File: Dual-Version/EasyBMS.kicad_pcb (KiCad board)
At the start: 2 copper layers, 48.8 x 100 mm, 174 parts, among them IC1 XL7046, IC2 LTC6811IG-1#PBF, IC3 ISO1042DWV, IC4 AMS1117-3.3, J1 TYPE-C-31-M-12, Q14 CJ2301, Q15 CJ2301, Q16 CJ2301, Q18 CJ2301, Q20 CJ2301, Q22 CJ2301, Q24 CJ2301, Q26 CJ2301, Q28 CJ2301, Q30 CJ2301, Q32 CJ2301, Q34 CJ2301, U1 ESP32-C6-MINI-1-N4, Y1 FC-135_32.7680KA-A5

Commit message: schematic improvements, parts changed, layout progress
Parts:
- removed CSLTC0, MISO0: SJ, EasyBMS:SJ_252
- removed IC3: ISO1042DWV, EasyBMS:SOIC127P1150X280-8N
- removed JP7: 2828XX-4282834-4, EasyBMS:TERMBLK_254-4N_16378166
- added B1: ~, RS485 Modul:RS-485-MODULE, F.Cu at (112.3, -18.5)
- added C18: 22uF, EasyBMS:C0805_334, F.Cu at (79.1, 54.8)
- added C22: 100nF, EasyBMS:C0402_334, F.Cu at (165.1, 15.1)
- added C30: 10nF, EasyBMS:C0402_334, F.Cu at (164.9, 127.2)
- added C32: 10nF, EasyBMS:C0402_334, F.Cu at (164.9, 121.3)
- added C34: 10nF, EasyBMS:C0402_334, F.Cu at (164.9, 115.4)
- added C36: 10nF, EasyBMS:C0402_334, F.Cu at (164.9, 109.5)
- added C38: 10nF, EasyBMS:C0402_334, F.Cu at (164.9, 103.6)
- added C40: 10nF, EasyBMS:C0402_334, F.Cu at (164.9, 97.7)
- added C42: 10nF, EasyBMS:C0402_334, F.Cu at (138.6, 96.1)
- added C44: 10nF, EasyBMS:C0402_334, F.Cu at (164.9, 91.8)
- added C46: 10nF, EasyBMS:C0402_334, F.Cu at (164.9, 85.9)
- added C48: 10nF, EasyBMS:C0402_334, F.Cu at (164.9, 80.0)
- added C49: 10nF, EasyBMS:C0402_334, F.Cu at (164.9, 74.1)
- added C50: 10nF, EasyBMS:C0402_334, F.Cu at (164.9, 68.2)
- added C51: 10nF, EasyBMS:C0402_334, F.Cu at (145.6, 94.8)
- added C52: 100nF, EasyBMS:C0805_334, F.Cu at (156.7, 109.9)
- added C53: 1uF, EasyBMS:C0402_334, F.Cu at (145.5, 98.8)
- added C54: 1uF, EasyBMS:C0402_334, F.Cu at (145.5, 100.1)
- added C55: 1uF, EasyBMS:C0402_334, F.Cu at (145.4, 101.3)
- added C56: 10nF, EasyBMS:C0402_334, F.Cu at (142.8, 104.8)
- added C57: 10nF, EasyBMS:C0805_334, F.Cu at (141.1, 100.2)
- added C58: 10nF, EasyBMS:C0805_334, F.Cu at (141.1, 102.2)
- added C59: 100nF, EasyBMS:C0805_334, F.Cu at (155.9, 114.8)
- added C61: 100nF, EasyBMS:C0402_334, F.Cu at (165.1, 19.2)
- added C62: 100nF, EasyBMS:C0402_334, F.Cu at (79.2, 30.0)
- added C64: 22uF, EasyBMS:C0805_334, F.Cu at (79.1, 57.9)
- added C65: 22uF, EasyBMS:C0805_334, F.Cu at (83.1, 29.9)
- added C66: 10nF, EasyBMS:C0402_334, F.Cu at (133.9, 93.3)
- added CAN-GNDP1: SJ, EasyBMS:SJ_252, F.Cu at (156.6, -22.3)
- added CAN-GNDV1: SJ, EasyBMS:SJ_252, F.Cu at (156.5, -17.6)
- added CAN-HP1: SJ, EasyBMS:SJ_252, F.Cu at (156.4, -14.0)
- added CAN-HV1: SJ, EasyBMS:SJ_252, F.Cu at (156.0, -10.2)
- added CAN-LP1: SJ, EasyBMS:SJ_252, F.Cu at (156.1, -6.30)
- added CAN-LV1: SJ, EasyBMS:SJ_252, F.Cu at (170.4, -16.8)
- added D17: ZMM5V6, EasyBMS:MELF-MLL34, F.Cu at (162.6, 133.1)
- added D19: ZMM5V6, EasyBMS:MELF-MLL34, F.Cu at (162.6, 127.2)
- added D21: ZMM5V6, EasyBMS:MELF-MLL34, F.Cu at (162.6, 121.3)
- added D23: ZMM5V6, EasyBMS:MELF-MLL34, F.Cu at (162.6, 115.4)
- added D25: ZMM5V6, EasyBMS:MELF-MLL34, F.Cu at (162.6, 109.5)
- added D26: ZMM5V6, EasyBMS:MELF-MLL34, F.Cu at (162.6, 103.6)
- added D27: ZMM5V6, EasyBMS:MELF-MLL34, F.Cu at (162.6, 97.7)
- added D28: ZMM5V6, EasyBMS:MELF-MLL34, F.Cu at (162.6, 91.8)
- added D29: ZMM5V6, EasyBMS:MELF-MLL34, F.Cu at (162.6, 85.9)
- added D30: ZMM5V6, EasyBMS:MELF-MLL34, F.Cu at (162.6, 80.0)
- added D31: ZMM5V6, EasyBMS:MELF-MLL34, F.Cu at (162.6, 74.1)
- added D32: ZMM5V6, EasyBMS:MELF-MLL34, F.Cu at (162.6, 68.2)
- added D33: SS210, EasyBMS:DO214AC_210, F.Cu at (156.0, 68.8)
- added D34: SS210, EasyBMS:DO214AC_210, F.Cu at (156.0, 71.3)
- added D35: PESD5V0L1BA, Diode_SMD:D_SOD-323, F.Cu at (161.0, 15.6)
- added D36: PESD5V0L1BA, Diode_SMD:D_SOD-323, F.Cu at (161.0, 18.5)
- added D37: LESD5D5.0CT1G, Diode_SMD:D_SOD-523, F.Cu at (72.8, 34.5)
- added D38: PESD5V0L1BA, Diode_SMD:D_SOD-323, F.Cu at (161.0, 21.5)
- added F1: 60V 100mA/JK-NSMD010, Resistor_SMD:R_1206_3216Metric, F.Cu at (169.9, 15.8)
- added F2: 60V 100mA/JK-NSMD010, Resistor_SMD:R_1206_3216Metric, F.Cu at (169.9, 19.1)
- added GND1: SJ, EasyBMS:SJ_252, F.Cu at (159.1, 66.4)
- added GND2: SJ, EasyBMS:SJ_252, F.Cu at (121.0, 136.2)
- added H4: MountingHole_Pad, MountingHole:MountingHole_6.5mm_Pad_Via, F.Cu at (151.6, 130.3)
- added H5: MountingHole_Pad, MountingHole:MountingHole_6.5mm_Pad_Via, F.Cu at (135.6, 130.3)
- added IC5: LTC6811IG-1, EasyBMS:SOP50P780X200-48N, F.Cu at (152.0, 100.6)
- added IC6: AMS1117-5, EasyBMS:SOT223_111, F.Cu at (79.3, -33.6)
- added IP-/GND1: SJ, EasyBMS:SJ_252, F.Cu at (124.8, 128.4)
- added J2: Screw_Terminal_01x04, TerminalBlock_TE-Connectivity:TerminalBlock_TE_282834-4_1x04_P2.54mm_Horizontal, F.Cu at (153.2, 18.0)
- added JP14: PINHD-1X2, EasyBMS:1X02, F.Cu at (186.2, 108.5)
- added JP15: PINHD-1X2, EasyBMS:1X02, F.Cu at (186.2, 105.5)
- added JP16: PINHD-1X2, EasyBMS:1X02, F.Cu at (186.2, 102.5)
- added JP17: PINHD-1X2, EasyBMS:1X02, F.Cu at (186.2, 99.5)
- added JP18: PINHD-1X2, EasyBMS:1X02, F.Cu at (186.2, 96.5)
- added JP19: PINHD-1X2, EasyBMS:1X02, F.Cu at (186.2, 93.5)
- added JP20: PINHD-1X2, EasyBMS:1X02, F.Cu at (186.2, 90.5)
- added JP21: PINHD-1X2, EasyBMS:1X02, F.Cu at (186.2, 87.5)
- added JP22: PINHD-1X2, EasyBMS:1X02, F.Cu at (186.2, 84.5)
- added JP23: PINHD-1X2, EasyBMS:1X02, F.Cu at (186.2, 81.5)
- added JP24: PINHD-1X2, EasyBMS:1X02, F.Cu at (186.2, 78.5)
- added Q1: CJ2301, EasyBMS:PG-SOT-23, F.Cu at (167.4, 133.1)
- added Q10: CJ2301, EasyBMS:PG-SOT-23, F.Cu at (167.4, 80.0)
- added Q11: CJ2301, EasyBMS:PG-SOT-23, F.Cu at (167.4, 74.1)
- added Q12: CJ2301, EasyBMS:PG-SOT-23, F.Cu at (167.4, 68.2)
- added Q13: NSV1C201MZ4, Package_TO_SOT_SMD:SOT-223, F.Cu at (150.1, 112.0)
- added Q2: CJ2301, EasyBMS:PG-SOT-23, F.Cu at (167.4, 127.2)
- added Q3: CJ2301, EasyBMS:PG-SOT-23, F.Cu at (167.4, 121.3)
- added Q4: CJ2301, EasyBMS:PG-SOT-23, F.Cu at (167.4, 115.4)
- added Q5: CJ2301, EasyBMS:PG-SOT-23, F.Cu at (167.4, 109.5)
- added Q6: CJ2301, EasyBMS:PG-SOT-23, F.Cu at (167.4, 103.6)
- added Q7: CJ2301, EasyBMS:PG-SOT-23, F.Cu at (167.4, 97.7)
- added Q8: CJ2301, EasyBMS:PG-SOT-23, F.Cu at (167.4, 91.8)
- added Q9: CJ2301, EasyBMS:PG-SOT-23, F.Cu at (167.4, 85.9)
- added R22: 49R9, EasyBMS:R0603_334, F.Cu at (135.4, 94.9)
- added R23: 1k, EasyBMS:R0603_334, F.Cu at (133.9, 97.7)
- added R24: 10k, EasyBMS:R0402_334, F.Cu at (141.1, 96.1)
- added R25: 10R0, EasyBMS:R1206_334, F.Cu at (178.6, 133.1)
- added R26: 10R0, EasyBMS:R1206_334, F.Cu at (178.6, 127.2)
- added R27: 10R0, EasyBMS:R1206_334, F.Cu at (178.6, 121.3)
- added R28: 10R0, EasyBMS:R1206_334, F.Cu at (178.6, 115.4)
- added R29: 10R0, EasyBMS:R1206_334, F.Cu at (178.6, 109.5)
- added R30: 10R0, EasyBMS:R1206_334, F.Cu at (178.6, 103.6)
- added R31: 10R0, EasyBMS:R1206_334, F.Cu at (178.6, 97.7)
- added R32: 10R0, EasyBMS:R1206_334, F.Cu at (178.6, 91.8)
- added R33: 10R0, EasyBMS:R1206_334, F.Cu at (178.6, 85.9)
- added R34: 10R0, EasyBMS:R1206_334, F.Cu at (178.6, 80.0)
- added R35: 10R0, EasyBMS:R1206_334, F.Cu at (178.6, 74.1)
- added R36: 10R0, EasyBMS:R1206_334, F.Cu at (178.6, 68.2)
- added R37: 10R0, EasyBMS:R1206_334, F.Cu at (171.4, 133.1)
- added R38: 10R0, EasyBMS:R1206_334, F.Cu at (171.4, 127.2)
- added R39: 10R0, EasyBMS:R1206_334, F.Cu at (171.4, 121.3)
- added R40: 10R0, EasyBMS:R1206_334, F.Cu at (171.4, 115.4)
- added R41: 10R0, EasyBMS:R1206_334, F.Cu at (171.4, 109.5)
- added R42: 10R0, EasyBMS:R1206_334, F.Cu at (171.4, 103.6)
- added R43: 10R0, EasyBMS:R1206_334, F.Cu at (171.4, 97.7)
- added R44: 10R0, EasyBMS:R1206_334, F.Cu at (171.4, 91.8)
- added R45: 10R0, EasyBMS:R1206_334, F.Cu at (171.4, 85.9)
- added R46: 10R0, EasyBMS:R1206_334, F.Cu at (171.4, 80.0)
- added R47: 10R0, EasyBMS:R1206_334, F.Cu at (171.4, 74.1)
- added R48: 10R0, EasyBMS:R1206_334, F.Cu at (171.4, 68.2)
- added R49: 100R, EasyBMS:R0402_334, F.Cu at (165.7, 135.2)
- added R50: 100R, EasyBMS:R0402_334, F.Cu at (165.7, 129.3)
- added R51: 100R, EasyBMS:R0402_334, F.Cu at (165.7, 123.4)
- added R52: 100R, EasyBMS:R0402_334, F.Cu at (165.7, 117.5)
- added R53: 100R, EasyBMS:R0402_334, F.Cu at (165.7, 111.6)
- added R54: 100R, EasyBMS:R0402_334, F.Cu at (165.7, 105.7)
- added R56: 100R, EasyBMS:R0402_334, F.Cu at (165.7, 99.8)
- added R62: 100R, EasyBMS:R0402_334, F.Cu at (165.7, 93.9)
- added R63: 100R, EasyBMS:R0402_334, F.Cu at (165.7, 88.0)
- added R64: 100R, EasyBMS:R0402_334, F.Cu at (165.7, 82.1)
- added R65: 100R, EasyBMS:R0402_334, F.Cu at (165.7, 76.2)
- added R66: 100R, EasyBMS:R0402_334, F.Cu at (165.7, 70.3)
- added R67: 3.3k, EasyBMS:R0402_334, F.Cu at (165.7, 131.0)
- added R68: 3.3k, EasyBMS:R0402_334, F.Cu at (165.7, 125.1)
- added R69: 3.3k, EasyBMS:R0402_334, F.Cu at (165.7, 119.2)
- added R70: 3.3k, EasyBMS:R0402_334, F.Cu at (165.7, 113.3)
- added R71: 3.3k, EasyBMS:R0402_334, F.Cu at (165.7, 107.4)
- added R72: 3.3k, EasyBMS:R0402_334, F.Cu at (165.7, 101.5)
- added R73: 3.3k, EasyBMS:R0402_334, F.Cu at (165.7, 95.6)
- added R74: 3.3k, EasyBMS:R0402_334, F.Cu at (165.7, 89.7)
- added R75: 3.3k, EasyBMS:R0402_334, F.Cu at (165.7, 83.8)
- added R76: 3.3k, EasyBMS:R0402_334, F.Cu at (165.7, 77.9)
- added R77: 3.3k, EasyBMS:R0402_334, F.Cu at (165.7, 72.0)
- added R78: 3.3k, EasyBMS:R0402_334, F.Cu at (165.7, 66.1)
- added R80: 100R, EasyBMS:R0402_334, F.Cu at (159.8, 69.1)
- added R81: 10k, EasyBMS:R0603_334, F.Cu at (182.1, 128.0)
- added R83: 10k NTC, EasyBMS:R0603_334, F.Cu at (182.1, 131.7)
- added R84: 12k, EasyBMS:R0402_334, F.Cu at (145.6, 97.0)
- added R85: 12k, EasyBMS:R0402_334, F.Cu at (145.6, 95.9)
- added R86: 10k, EasyBMS:R0603_334, F.Cu at (182.2, 79.6)
- added R87: 10k NTC, EasyBMS:R0603_334, F.Cu at (182.2, 76.4)
- added R88: 100R, EasyBMS:R0402_334, F.Cu at (156.2, 108.2)
- added R89: 1k, EasyBMS:R0603_334, F.Cu at (145.4, 107.8)
- added R90: 100R, EasyBMS:R0603_334, F.Cu at (144.9, 110.4)
- added R91: 1k, EasyBMS:R0603_334, F.Cu at (143.3, 107.8)
- added R92: 49R9, EasyBMS:R0603_334, F.Cu at (144.9, 105.0)
- added R93: 49R9, EasyBMS:R0603_334, F.Cu at (144.9, 102.9)
- added RS485-AP1: SJ, EasyBMS:SJ_252, F.Cu at (170.4, -13.6)
- added RS485-BP1: SJ, EasyBMS:SJ_252, F.Cu at (170.4, -10.4)
- added RS485-GNDPWR1: SJ, EasyBMS:SJ_252, F.Cu at (157.1, 51.8)
- added RS485-VDD1: SJ, EasyBMS:SJ_252, F.Cu at (170.4, -4.08)
- added U2: ACS770xCB-100B-PFF, Sensor_Current:Allegro_CB_PFF, B.Cu at (137.9, 98.3)
- added U3: ADuM1201BR, Package_SO:SOIC-8_3.9x4.9mm_P1.27mm, F.Cu at (70.8, 30.1)
- added U4: RJ-064-1, RJ45 Connectors:CONN-SMD_RJ-064, F.Cu at (149.0, 44.7)
- added U5: CA-IS3050CG, Package_SO:SOIC-8_7.5x5.85mm_P1.27mm, F.Cu at (143.9, 20.5)
- added U6: RJ-064-1, RJ45 Connectors:CONN-SMD_RJ-064, F.Cu at (165.3, 44.7)
- added U7: TME-0305S, Converter_DCDC:Converter_DCDC_TRACO_TME_03xxS_05xxS_12xxS_Single_THT, F.Cu at (129.2, 20.2)
- C12: value 47µF -> 22uF; footprint EasyBMS:C1206_334 -> EasyBMS:C0805_334
- C2: value 100µF/16V -> 10uF; footprint EasyBMS:153CLV-0605_334 -> Capacitor_SMD:C_0805_2012Metric
- C3: value 100nF -> 10nF
- C7: value 1uF -> 22uF; footprint EasyBMS:C0402_334 -> EasyBMS:C0805_334
- IC2: value LTC6811IG-1#PBF -> LTC6811IG-1
- R1: value 100R -> 49R9
- R17: value 20k -> 1k
- R59: value 600R@100MHz -> 100R
- moved C11 118.1 mm to (148.6, 24.3)
- moved R12 117.9 mm to (150.2, 28.7)
- moved TERM0 117.8 mm to (152.6, 28.7)
- moved C10 114.5 mm to (136.1, 20.4)
- moved H2 110.9 mm to (186.3, 41.5)
- moved C2 109.9 mm to (96.9, 15.8)
- moved D7 65.9 mm to (124.2, 133.8), turned to 180 degrees
- moved C12 65.7 mm to (129.7, 89.5), turned to 180 degrees
- moved D1 62.4 mm to (124.2, 131.3), turned to 0 degrees
- moved C3 50.3 mm to (164.9, 133.1)
- moved R59 41.1 mm to (156.4, 112.7), turned to 180 degrees
- moved R1 40.4 mm to (132.4, 94.9), turned to 180 degrees
- moved R57 38.5 mm to (134.6, 105.6)
- moved R4 38.1 mm to (98.0, 70.9)
- moved R7 38.1 mm to (98.0, 123.0)
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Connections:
- net +5V/1 renamed +12V
- net /C0 renamed /Cell Pack 1/C0
- net /C1 renamed /Cell Pack 1/C1
- net /C1+ renamed /Cell Pack 1/C1+
- net /C10 renamed /Cell Pack 1/C10
- net /C10+ renamed /Cell Pack 1/C10+
- net /C11 renamed /Cell Pack 1/C11
- net /C11+ renamed /Cell Pack 1/C11+
- net /C12 renamed /Cell Pack 1/C12
- net /C12+ renamed /Cell Pack 1/C12+
- net /C2 renamed /Cell Pack 1/C2
- net /C2+ renamed /Cell Pack 1/C2+
- net /C3 renamed /Cell Pack 1/C3
- net /C3+ renamed /Cell Pack 1/C3+
- net /C4 renamed /Cell Pack 1/C4
- net /C4+ renamed /Cell Pack 1/C4+
- net /C5 renamed /Cell Pack 1/C5
- net /C5+ renamed /Cell Pack 1/C5+
- net /C6 renamed /Cell Pack 1/C6
- net /C6+ renamed /Cell Pack 1/C6+
- net /C7 renamed /Cell Pack 1/C7
- net /C7+ renamed /Cell Pack 1/C7+
- net /C8 renamed /Cell Pack 1/C8
- net /C8+ renamed /Cell Pack 1/C8+
- net /C9 renamed /Cell Pack 1/C9
- net /C9+ renamed /Cell Pack 1/C9+
- net /CSLTC renamed CSLTC
- net /IPB renamed /Cell Pack 1/IPB
- net /MISO renamed MISO
- net /MOSI renamed MOSI
- net /S1 renamed /Cell Pack 1/S1
- net /S10 renamed /Cell Pack 1/S10
- net /S11 renamed /Cell Pack 1/S11
- net /S12 renamed /Cell Pack 1/S12
- net /S2 renamed /Cell Pack 1/S2
- net /S3 renamed /Cell Pack 1/S3
- net /S4 renamed /Cell Pack 1/S4
- net /S5 renamed /Cell Pack 1/S5
- net /S6 renamed /Cell Pack 1/S6
- net /S7 renamed /Cell Pack 1/S7
- net /S8 renamed /Cell Pack 1/S8
- net /S9 renamed /Cell Pack 1/S9
- net /SCLK renamed SCLK
- net /V+ renamed /Cell Pack 1/V+
- net /VREF1 renamed /Cell Pack 1/VREF1
- net /VREF2 renamed /Cell Pack 1/VREF2
- net /VTEMP2 renamed /Cell Pack 1/VTEMP2
- C1 pad 2: /GND2 -> GND
- C11 pad 1: Net-(IC3-VCC2) -> Net-(D37-K)
- C11 pad 2: Net-(IC3-GND2) -> Net-(D35-A1)
- C12 pad 1: Net-(IC3-VCC2) -> +5V
- C12 pad 2: Net-(IC3-GND2) -> GND
- C19 pad 2: /GND2 -> GND
- C20 pad 1: /GND2 -> GND
- C23 pad 2: /GND2 -> GND
- C25 pad 2: /C1- -> /Cell Pack 1/C1-
- C3 pad 1: /GND2 -> /Cell Pack 2/C12
- C3 pad 2: GND -> /Cell Pack 2/C11
- C4 pad 2: /GND2 -> GND
- D1 pad A: /GND2 -> GND
- D1 pad C: GND -> /Cell Pack 1/C1-
- D4 pad 2: /C1- -> /Cell Pack 1/C1-
- D7 pad A: GND -> /Cell Pack 1/C1-
- D7 pad C: /GND2 -> GND
- IC2 pad 27: /VTEMP1 -> /Cell Pack 1/CURRENTSENSE
- IC2 pad 29: /VTEMPSOUTH -> /Cell Pack 1/VTEMP1
- IC2 pad 30: /GND2 -> GND
- IC2 pad 31: /GND2 -> GND
- IC2 pad 32: /VTEMPNORTH -> /Cell Pack 1/VTEMPSOUTH
- IC2 pad 33: /GPIO5 -> /Cell Pack 1/VTEMPNORTH
- IC2 pad 38: unconnected-(IC2-DRIVE-Pad38) -> /Cell Pack 1/DRIVE
- IC2 pad 40: /GND2 -> GND
- IC2 pad 45: /IBIAS -> Net-(IC2-IBIAS)
- IC2 pad 46: /IBIAS -> Net-(IC2-ICMP)
- IC2 pad 47: /IMB -> /Cell Pack 1/IMB
- JP11 pad 1: /C1- -> /Cell Pack 1/C1-
- JP13 pad 1: /VTEMP1 -> /Cell Pack 1/VTEMP1
- R1 pad 1: /IMB -> Net-(C66-Pad1)
- R17 pad 1: /GND2 -> GND
- R17 pad 2: /IBIAS -> Net-(IC2-ICMP)
- R3 pad 1: /VTEMPNORTH -> /Cell Pack 1/VTEMPNORTH
- R4 pad 1: /GND2 -> GND
- R4 pad 2: /VTEMPNORTH -> /Cell Pack 1/VTEMPNORTH
- R57 pad 1: /GND2 -> GND
- R57 pad 2: /VTEMP1 -> /Cell Pack 1/VTEMP1
- R58 pad 1: /GND2 -> GND
- R59 pad 1: /C1- -> /Cell Pack 2/C12+POWER
- R59 pad 2: /GND2 -> Net-(C59-Pad2)
- R60 pad 2: /C1- -> /Cell Pack 1/C1-
- R7 pad 1: /VTEMPSOUTH -> /Cell Pack 1/VTEMPSOUTH
- R8 pad 1: /GND2 -> GND
- R8 pad 2: /VTEMPSOUTH -> /Cell Pack 1/VTEMPSOUTH
- R82 pad 1: /C1- -> /Cell Pack 1/C1-
- U1 pad 26: unconnected-(U1-IO20-Pad26) -> Net-(U1-IO20)
- U1 pad 27: unconnected-(U1-IO21-Pad27) -> Net-(U1-IO21)
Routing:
- net /Cell Pack 2/VREF2: track 0.00 -> 96.3 mm, vias 0 -> 5
- net GND: track 146.5 -> 52.2 mm, vias 129 -> 205
- net /Cell Pack 2/C12+: track 0.00 -> 83.5 mm, vias 0 -> 1
- net /Cell Pack 2/C12+POWER: track 0.00 -> 77.1 mm
- net Net-(U1-IO23): track 105.1 -> 29.2 mm, vias 2 -> 1
- net Net-(U1-IO22): track 102.9 -> 28.8 mm, vias 2 -> 1
- net +3V3: track 147.0 -> 78.4 mm
- net /Cell Pack 1/VTEMPNORTH: track 0.00 -> 65.9 mm, vias 0 -> 2
- net /Cell Pack 2/VTEMPSOUTH: track 0.00 -> 65.9 mm, vias 0 -> 2
- net /VTEMPNORTH: track 65.7 -> 0.00 mm, vias 2 -> 0
- net /Cell Pack 2/VTEMP2: track 0.00 -> 64.1 mm, vias 0 -> 1
- net /VTEMP1: track 63.7 -> 0.00 mm, vias 1 -> 0
- net /Cell Pack 2/VTEMP1: track 0.00 -> 57.1 mm, vias 0 -> 1
- net /Cell Pack 1/VTEMP1: track 0.00 -> 57.1 mm, vias 0 -> 1
- net /Cell Pack 2/C1-: track 0.00 -> 54.5 mm, vias 0 -> 2
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- added copper zone on B.Cu, net GND1
- added copper zone on F.Cu, net GND1
- added copper zone on B.Cu, net Net-(R25-Pad2)
- added copper zone on F.Cu, net Net-(R25-Pad2)
- added copper zone on B.Cu, net Net-(R26-Pad2)
- added copper zone on F.Cu, net Net-(R26-Pad2)
- added copper zone on B.Cu, net Net-(R27-Pad2)
- added copper zone on F.Cu, net Net-(R27-Pad2)
- added copper zone on B.Cu, net Net-(R28-Pad2)
- added copper zone on F.Cu, net Net-(R28-Pad2)
- added copper zone on B.Cu, net Net-(R29-Pad2)
- added copper zone on F.Cu, net Net-(R29-Pad2)
- added copper zone on B.Cu, net Net-(R30-Pad2)
- added copper zone on F.Cu, net Net-(R30-Pad2)
- added copper zone on B.Cu, net Net-(R31-Pad2)
- added copper zone on F.Cu, net Net-(R31-Pad2)
- added copper zone on B.Cu, net Net-(R32-Pad2)
- added copper zone on F.Cu, net Net-(R32-Pad2)
- added copper zone on B.Cu, net Net-(R33-Pad2)
- added copper zone on F.Cu, net Net-(R33-Pad2)
- added copper zone on B.Cu, net Net-(R34-Pad2)
- added copper zone on F.Cu, net Net-(R34-Pad2)
- added copper zone on B.Cu, net Net-(R35-Pad2)
- added copper zone on F.Cu, net Net-(R35-Pad2)
- added copper zone on B.Cu, net Net-(R36-Pad2)
- added copper zone on F.Cu, net Net-(R36-Pad2)
- removed copper zone on B.Cu, net /GND2
- removed copper zone on F.Cu, net /GND2
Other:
- board size 48.8 x 100 mm -> 100 x 100 mm

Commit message: schematic and layout finalized, production data generated
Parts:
- removed D36, D38: PESD5V0L1BA, Diode_SMD:D_SOD-323
- removed U4, U6: RJ-064-1, RJ45 Connectors:CONN-SMD_RJ-064
- added C60: 1nF/2000V, EasyBMS:C1206_334, F.Cu at (163.7, 47.8)
- added H6: MOUNT-HOLE3.2, EasyBMS:3,2_237, F.Cu at (187.9, 135.0)
- added L2: 10uH, Resistor_SMD:R_0805_2012Metric, F.Cu at (140.6, 72.4)
- added R61: 1M, EasyBMS:R1206_334, F.Cu at (161.7, 47.8)
- added RJ1: MJ88-B211-JRS3, EasyEDA2KiCAD:RJ45-SMD_HELING_MJ88-B211-JRS3, F.Cu at (152.8, 46.6)
- added RJ2: MJ88-B211-JRS3, EasyEDA2KiCAD:RJ45-SMD_HELING_MJ88-B211-JRS3, F.Cu at (172.6, 46.6)
- B1, RS485-AP1, RS485-BP1: moved to B.Cu
- D11, D13, D9: value LESD5D5.0CT1G -> LESD5D5.0CT1G_C5199850; footprint EasyBMS:SOD523_210 -> EasyEDA2KiCAD:SOD-523_L1.2-W0.8-LS1.6-BI
- D35: value PESD5V0L1BA -> PESD1CAN,215; footprint Diode_SMD:D_SOD-323 -> EasyEDA2KiCAD:SOT-23_L2.9-W1.3-P1.90-LS2.4-BR
- D37: value LESD5D5.0CT1G -> LESD5D5.0CT1G_C5199850; footprint Diode_SMD:D_SOD-523 -> EasyEDA2KiCAD:SOD-523_L1.2-W0.8-LS1.6-BI
- IC1: footprint EasyBMS:SOIC127P600X170-9N -> EasyEDA2KiCAD:ESOP-8_L4.9-W3.9-P1.27-LS6.0-TL-EP
- LED2: footprint EasyBMS:XL-1615RGBC-WS2812B -> EasyEDA2KiCAD:LED-SMD_4P-L1.6-W1.5_XL-1615RGBC-WS2812B-1
- moved D37 111.3 mm to (182.2, 55.0), turned to -90 degrees
- moved IC6 95.1 mm to (138.5, 40.9), turned to 90 degrees
- moved U3 88.0 mm to (142.4, 81.1)
- moved B1 85.5 mm to (159.1, 53.0)
- moved C22 85.2 mm to (138.7, 96.1), turned to 180 degrees
- moved C62 82.1 mm to (145.8, 77.8)
- moved CAN-GNDP1 81.9 mm to (173.0, 58.0), turned to -90 degrees
- moved CAN-GNDV1 79.1 mm to (179.6, 58.0), turned to -90 degrees
- moved CAN-HP1 75.0 mm to (177.4, 58.0), turned to -90 degrees
- moved CAN-LV1 74.8 mm to (168.6, 58.0), turned to -90 degrees
- moved C18 73.5 mm to (152.4, 59.9), turned to -90 degrees
- moved C2 73.0 mm to (140.6, 74.4), turned to 180 degrees
- moved CAN-HV1 69.8 mm to (170.8, 58.0), turned to -90 degrees
- moved CAN-LP1 67.1 mm to (175.2, 58.0), turned to -90 degrees
- moved RS485-VDD1 65.9 mm to (146.7, 57.4)
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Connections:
- B1 pad 0V: GNDPWR -> Earth
- C11 pad 1: Net-(D37-K) -> Net-(J2-Pin_1)
- C11 pad 2: Net-(D35-A1) -> Net-(J2-Pin_4)
- C18 pad 1: Net-(D37-K) -> Net-(J2-Pin_1)
- C18 pad 2: Net-(D35-A1) -> Net-(J2-Pin_4)
- C2 pad 1: +3V3 -> +12V
- CAN-GNDP1 pad 2: Net-(D35-A1) -> Net-(J2-Pin_4)
- CAN-GNDV1 pad 2: Net-(D35-A1) -> Net-(J2-Pin_4)
- D35 pad 1: Net-(D35-A1) -> Net-(U5-CANH)
- D37 pad 1: Net-(D37-K) -> Net-(J2-Pin_4)
- D37 pad 2: Net-(D35-A1) -> Net-(J2-Pin_1)
- F1 pad 1: Net-(D36-A2) -> Net-(U5-CANH)
- J2 pad 1: Net-(D37-K) -> Net-(J2-Pin_1)
- J2 pad 4: Net-(D35-A1) -> Net-(J2-Pin_4)
- RS485-GNDPWR1 pad 1: Net-(D35-A1) -> Net-(J2-Pin_4)
- RS485-VDD1 pad 2: Net-(D37-K) -> Net-(J2-Pin_1)
- TERM0 pad 1: Net-(D36-A2) -> Net-(U5-CANH)
- U5 pad 5: Net-(D35-A1) -> Net-(J2-Pin_4)
- U5 pad 7: Net-(D36-A2) -> Net-(U5-CANH)
- U5 pad 8: Net-(D37-K) -> Net-(J2-Pin_1)
- U7 pad 2: +3V3 -> Net-(U7-+Vin)
- U7 pad 3: Net-(D35-A1) -> Net-(J2-Pin_4)
- U7 pad 4: Net-(D37-K) -> Net-(J2-Pin_1)
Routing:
- net Net-(J2-Pin_1): track 0.00 -> 63.8 mm, vias 0 -> 4
- net Net-(U1-IO21): track 0.00 -> 54.1 mm, vias 0 -> 2
- net VDD: track 0.00 -> 53.8 mm, vias 0 -> 3
- net Net-(U1-IO20): track 0.00 -> 53.1 mm, vias 0 -> 2
- net Net-(B1-PadA+): track 0.00 -> 48.3 mm, vias 0 -> 1
- net Net-(B1-PadB-): track 0.00 -> 47.4 mm, vias 0 -> 1
- net GND1: track 42.6 -> 0.08 mm, vias 57 -> 89
- net GNDPWR: track 0.00 -> 40.4 mm, vias 0 -> 3
- net Net-(J2-Pin_2): track 0.00 -> 38.7 mm, vias 0 -> 2
- net Net-(U3-VIA): track 0.00 -> 38.5 mm, vias 0 -> 1
- net Net-(U3-VOB): track 0.00 -> 37.3 mm, vias 0 -> 1
- net Net-(J2-Pin_3): track 0.00 -> 34.2 mm, vias 0 -> 2
- net +3V3: track 78.4 -> 111.9 mm
- net +12V: track 111.7 -> 143.2 mm, vias 4 -> 8
- net /Cell Pack 1/CURRENTSENSE: track 0.95 -> 23.6 mm, vias 0 -> 2
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- added copper zone on B.Cu, net Earth
- added copper zone on F.Cu, net Earth
- added copper zone on F.Cu, net GNDPWR
- added copper zone on F.Cu, net Net-(J2-Pin_4)
- added copper zone on B.Cu, net Net-(U2-IP+)
- added copper zone on F.Cu, net Net-(U2-IP+)
- added copper zone on B.Cu, net Net-(U2-IP-)
- added copper zone on F.Cu, net Net-(U2-IP-)
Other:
- board text added: "CAN-PL"
- board text added: "CAN-VC"
- board text added: "EasyBMS Dual v3.1 17.05.2025"
- board text added: "RS485 PL"
- board text added: "RS485-PWR5V"
- board text added: "VE.Bus"
- board text added: "VE.CAN/ Pylontech"
- board text removed: "EasyBMS MEB v3.0 22.02.2025"

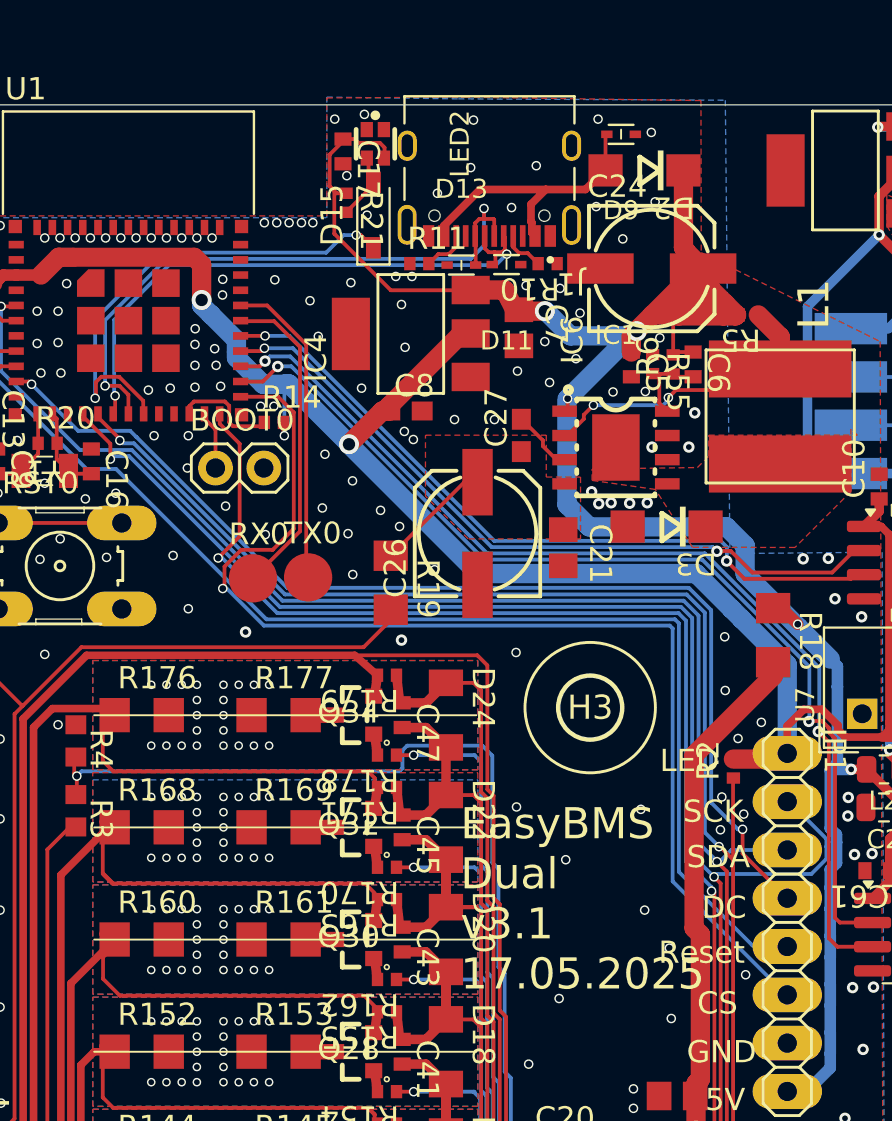
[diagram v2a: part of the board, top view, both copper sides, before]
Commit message: new RGB LED and additional simple red LED
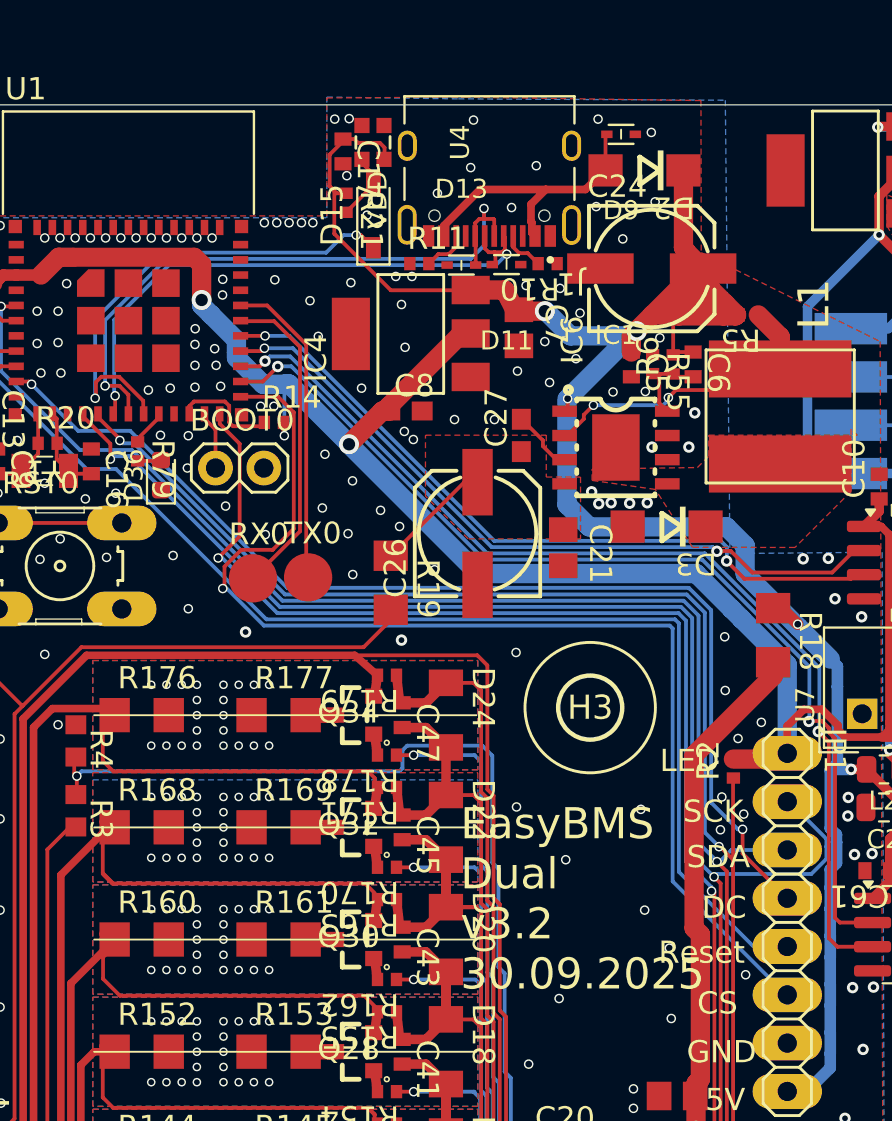
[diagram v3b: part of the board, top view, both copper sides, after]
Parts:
- removed LED2: XL-1615RGBC-WS2812B, EasyEDA2KiCAD:LED-SMD_4P-L1.6-W1.5_XL-1615RGBC-WS2812B-1
- added D36: LED, LED_SMD:LED_0603_1608Metric, F.Cu at (102.5, 56.9)
- added R79: 1k, EasyBMS:R0402_334, F.Cu at (101.3, 55.6)
- added U4: XL-0807RGBC-WS2812B, EasyEDA2KiCAD:LED-SMD_4P-L2.0-W1.8_XL-0807RGBC-WS2812B, F.Cu at (113.7, 39.4)
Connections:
- U1 pad 20: unconnected-(U1-IO15-Pad20) -> /LED
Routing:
- net /LED: track 0.00 -> 1.94 mm
- net Net-(D36-A): track 0.00 -> 1.24 mm
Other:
- board text added: "EasyBMS Dual v3.2 30.09.2025"
- board text removed: "EasyBMS Dual v3.1 17.05.2025"
